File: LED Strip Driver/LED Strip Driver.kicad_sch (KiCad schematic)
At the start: 9 parts, among them J1 PWM CTRL, J2 LOAD+, J3 LOAD-, U1 TPS92360

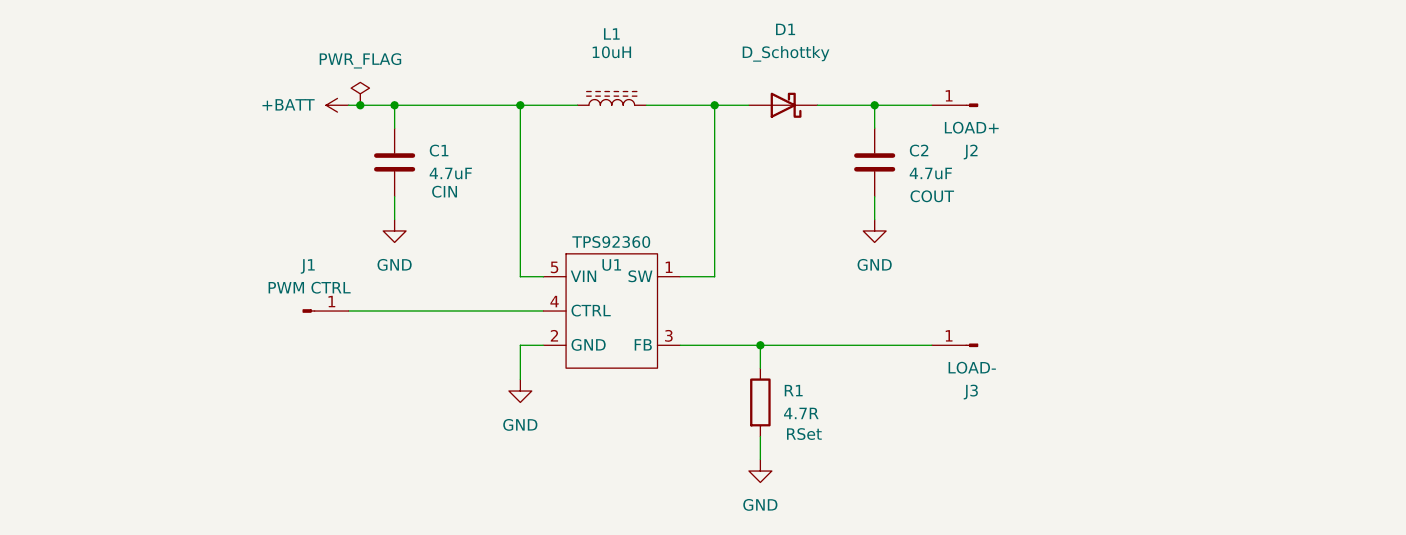
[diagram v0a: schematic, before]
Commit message: complete pcb for led driver
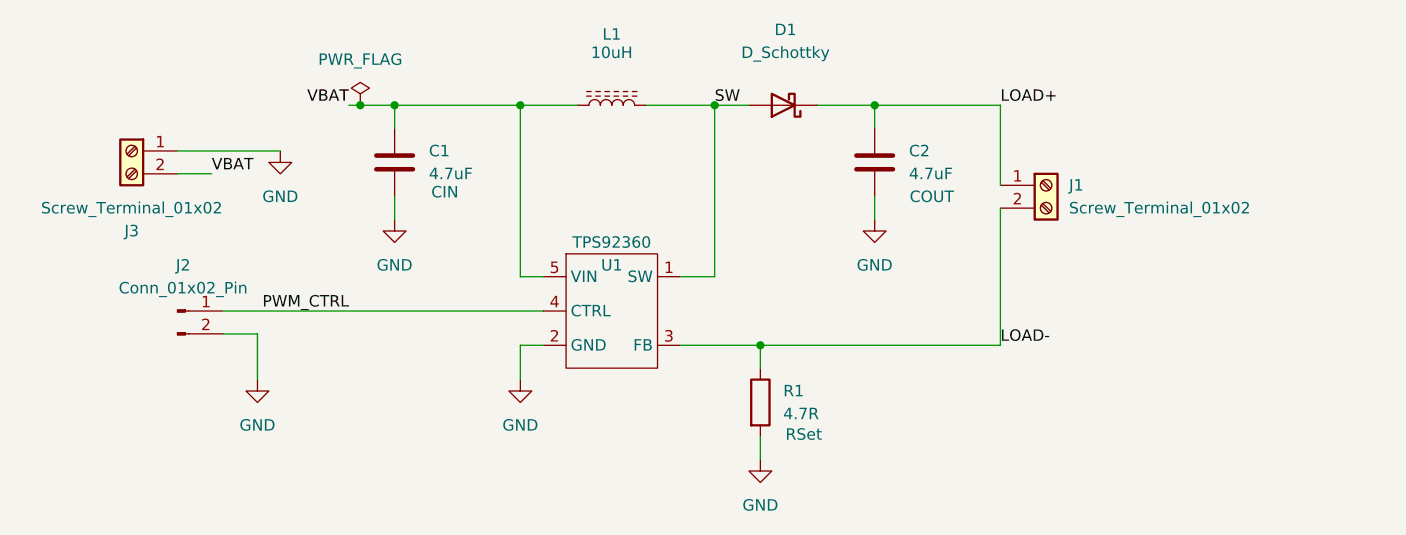
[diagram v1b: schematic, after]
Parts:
- removed J1: PWM CTRL, symbol Connector:Conn_01x01_Pin
- removed J2: LOAD+, symbol Connector:Conn_01x01_Pin
- removed J3: LOAD-, symbol Connector:Conn_01x01_Pin
- added J1, J3: Screw_Terminal_01x02, TerminalBlock_Phoenix:TerminalBlock_Phoenix_PT-1,5-2-5.0-H_1x02_P5.00mm_Horizontal, symbol Connector:Screw_Terminal_01x02
- added J2: Conn_01x02_Pin, Connector_PinHeader_2.54mm:PinHeader_1x02_P2.54mm_Vertical, symbol Connector:Conn_01x02_Pin
- C1, C2: footprint (none) -> Capacitor_SMD:C_0805_2012Metric_Pad1.18x1.45mm_HandSolder
- D1: footprint (none) -> Diode_SMD:D_SOD-323_HandSoldering; Part NSR0240 -> NSR0240HT1G
- L1: footprint (none) -> Inductor_SMD:L_Coilcraft_LPS4018; Part LPS4018-103ML -> LPS4018-103MRC
- R1: footprint (none) -> Resistor_SMD:R_0805_2012Metric_Pad1.20x1.40mm_HandSolder
- U1: footprint (none) -> LED Strip Driver Footprints:SOT65P210X110-5N
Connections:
- net GND: now also J2.2 (Pin_2), J3.1 (Pin_1)
- net SW: now reaches D1.2 (A), L1.2, U1.1 (SW)
- net LOAD-: now reaches R1.1, U1.3 (FB)
- net LOAD-: now also J1.2 (Pin_2)
- net PWM_CTRL: now reaches U1.4 (CTRL)
- net PWM_CTRL: now also J2.1 (Pin_1)
- net LOAD+: now reaches C2.1, D1.1 (K)
- net LOAD+: now also J1.1 (Pin_1)
- net +BATT renamed VBAT
- net VBAT: now also J3.2 (Pin_2)

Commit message: flip pwm connector so gnd pad is square
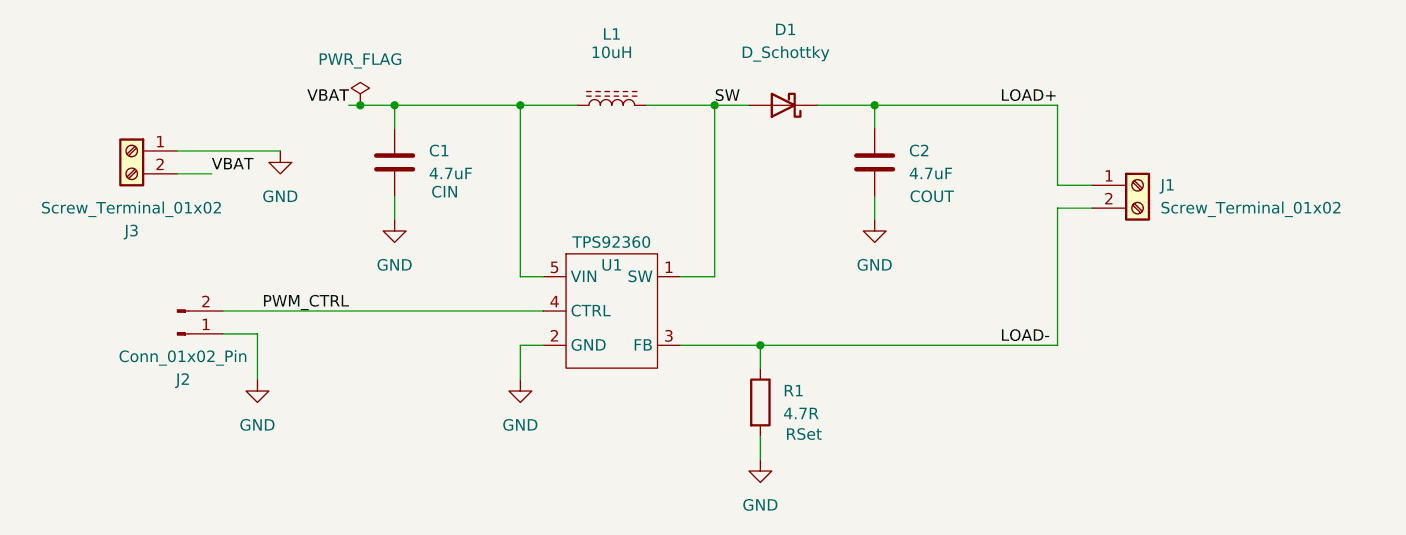
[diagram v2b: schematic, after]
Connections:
- net GND: now also J2.1 (Pin_1); no longer J2.2 (Pin_2)
- net PWM_CTRL: now also J2.2 (Pin_2); no longer J2.1 (Pin_1)
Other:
- moved on the sheet: J1
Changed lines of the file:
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@@
 	(wire
 		(pts
-			(xy 173.99 50.8) (xy 173.99 59.69)
+			(xy 180.34 59.69) (xy 184.15 59.69)
+		)
+		(stroke
+			(width 0)
+			(type default)
+		)
+	)
+	(wire
+		(pts
+			(xy 180.34 50.8) (xy 180.34 59.69)
+		)
+		(stroke
+			(width 0)
+			(type default)
+		)
+	)
+	(wire
+		(pts
+			(xy 180.34 62.23) (xy 180.34 77.47)
 		)
 		(stroke
@@
 	(wire
 		(pts
+			(xy 87.63 73.66) (xy 123.19 73.66)
+		)
+		(stroke
+			(width 0)
+			(type default)
+		)
+	)
+	(wire
+		(pts
+			(xy 91.44 76.2) (xy 91.44 81.28)
+		)
+		(stroke
+			(width 0)
+			(type default)
+		)
+	)
+	(wire
+		(pts
 			(xy 123.19 69.85) (xy 120.65 69.85)
 		)
@@
 	(wire
 		(pts
+			(xy 87.63 76.2) (xy 91.44 76.2)
+		)
+		(stroke
+			(width 0)
+			(type default)
+		)
+	)
+	(wire
+		(pts
 			(xy 106.68 60.96) (xy 106.68 63.5)
 		)
@@
 	(wire
 		(pts
-			(xy 147.32 77.47) (xy 173.99 77.47)
+			(xy 147.32 77.47) (xy 180.34 77.47)
 		)
 		(stroke
@@
 	(wire
 		(pts
-			(xy 173.99 62.23) (xy 173.99 77.47)
-		)
-		(stroke
-			(width 0)
-			(type default)
-		)
-	)
-	(wire
-		(pts
 			(xy 147.32 87.63) (xy 147.32 90.17)
 		)
@@
 	(wire
 		(pts
-			(xy 160.02 50.8) (xy 173.99 50.8)
+			(xy 160.02 50.8) (xy 180.34 50.8)
 		)
 		(stroke
@@
 	(wire
 		(pts
-			(xy 91.44 76.2) (xy 91.44 81.28)
-		)
-		(stroke
-			(width 0)
-			(type default)
-		)
-	)
-	(wire
-		(pts
 			(xy 106.68 50.8) (xy 120.65 50.8)
 		)
@@
 	(wire
 		(pts
+			(xy 180.34 62.23) (xy 184.15 62.23)
+		)
+		(stroke
+			(width 0)
+			(type default)
+		)
+	)
+	(wire
+		(pts
 			(xy 102.87 50.8) (xy 106.68 50.8)
 		)
@@
 	(wire
 		(pts
-			(xy 87.63 73.66) (xy 123.19 73.66)
-		)
-		(stroke
-			(width 0)
-			(type default)
-		)
-	)
-	(wire
-		(pts
 			(xy 160.02 60.96) (xy 160.02 63.5)
 		)
@@
 		(pts
 			(xy 160.02 50.8) (xy 160.02 53.34)
-		)
-		(stroke
-			(width 0)
-			(type default)
-		)
-	)
-	(wire
-		(pts
-			(xy 87.63 76.2) (xy 91.44 76.2)
 		)
 		(stroke
@@
 	(symbol
 		(lib_id "Connector:Conn_01x02_Pin")
-		(at 82.55 73.66 0)
+		(at 82.55 76.2 0)
+		(mirror x)
 		(unit 1)
 		(exclude_from_sim no)
@@
 		(fields_autoplaced yes)
 		(property "Reference" "J2"
-			(at 83.185 68.58 0)
+			(at 83.185 81.28 0)
 			(effects
 				(font
@@
 		)
 		(property "Value" "Conn_01x02_Pin"
-			(at 83.185 71.12 0)
+			(at 83.185 78.74 0)
 			(effects
 				(font
@@
 		)
 		(property "Footprint" "Connector_PinHeader_2.54mm:PinHeader_1x02_P2.54mm_Vertical"
-			(at 82.55 73.66 0)
+			(at 82.55 76.2 0)
 			(effects
 				(font
@@
 		)
 		(property "Datasheet" "~"
-			(at 82.55 73.66 0)
+			(at 82.55 76.2 0)
 			(effects
 				(font
@@
 		)
 		(property "Description" "Generic connector, single row, 01x02, script generated"
-			(at 82.55 73.66 0)
+			(at 82.55 76.2 0)
 			(effects
 				(font
@@
 	(symbol
 		(lib_id "Connector:Screw_Terminal_01x02")
-		(at 179.07 59.69 0)
+		(at 189.23 59.69 0)
 		(unit 1)
 		(exclude_from_sim no)
@@
 		(fields_autoplaced yes)
 		(property "Reference" "J1"
-			(at 181.61 59.6899 0)
+			(at 191.77 59.6899 0)
 			(effects
 				(font
@@
 		)
 		(property "Value" "Screw_Terminal_01x02"
-			(at 181.61 62.2299 0)
+			(at 191.77 62.2299 0)
 			(effects
 				(font
@@
 		)
 		(property "Footprint" "TerminalBlock_Phoenix:TerminalBlock_Phoenix_PT-1,5-2-5.0-H_1x02_P5.00mm_Horizontal"
-			(at 179.07 59.69 0)
+			(at 189.23 59.69 0)
 			(effects
 				(font
@@
 		)
 		(property "Datasheet" "~"
-			(at 179.07 59.69 0)
+			(at 189.23 59.69 0)
 			(effects
 				(font
@@
 		)
 		(property "Description" "Generic screw terminal, single row, 01x02, script generated (kicad-library-utils/schlib/autogen/connector/)"
-			(at 179.07 59.69 0)
-			(effects
-				(font
+			(at 189.23 59.69 0)
+			(effects
+				(font
